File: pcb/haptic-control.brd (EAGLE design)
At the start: 40 x 160 mm, 134 parts, among them M1 SPH0641LM4H-1, P1 2P-PAD_1X3.5, P2 2P-PAD_1X3.5, P3 2P-PAD_1X3.5, P4 2P-PAD_1X3.5, U1 MIC23159, U10 DRV2605L, U11 DRV2605L, U12 MTCH6301, U2 BQ51050B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

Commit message: silkscreen experiments
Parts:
- moved U$3 1.80 mm to (35.5, 16.0)
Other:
- outline, holes or cut-outs redrawn
- board text added: "HapticControl V0.1 1920"
- board text removed: "1920"

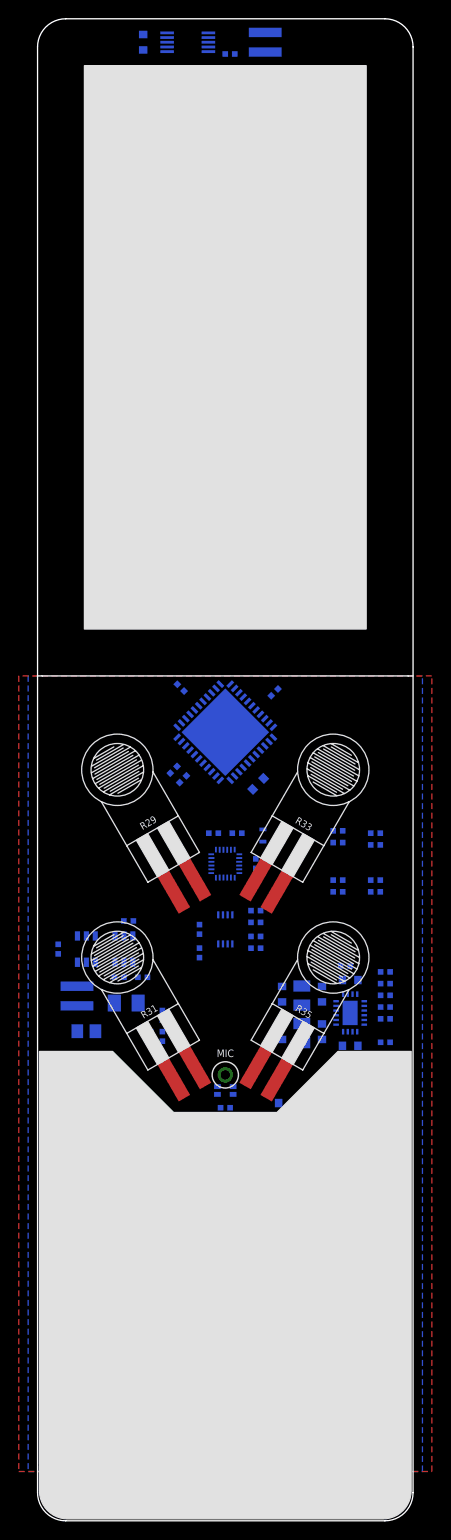
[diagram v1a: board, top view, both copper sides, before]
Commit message: Add pcap touch panel
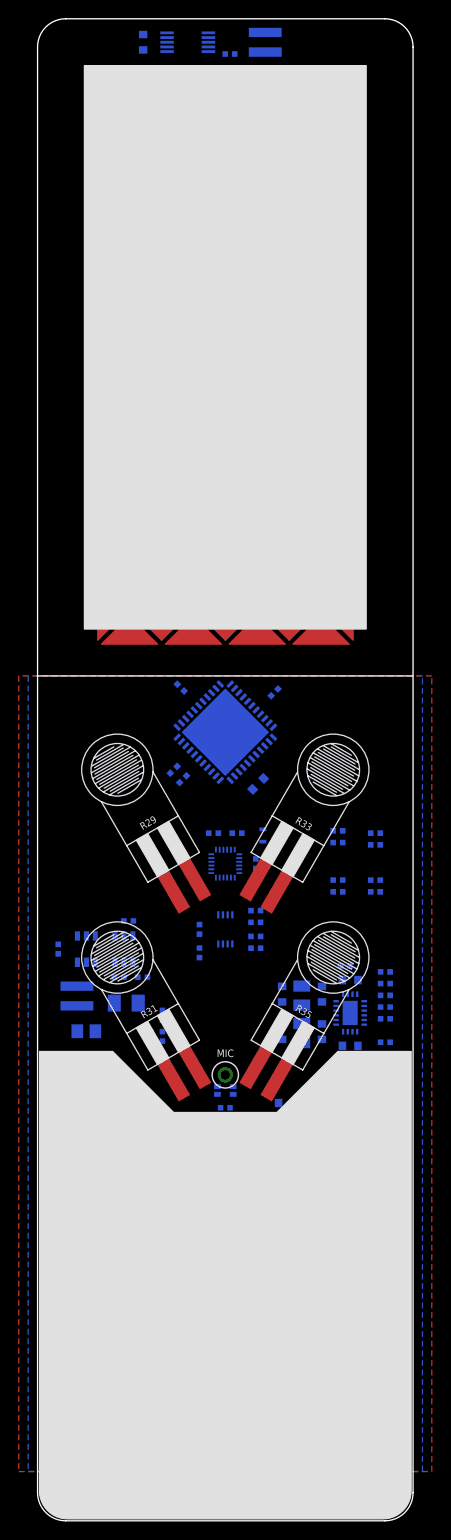
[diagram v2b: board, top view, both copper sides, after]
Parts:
- added MAT-X1, MAT-X2, MAT-X3, MAT-X4: X_9P, Touch Panel:TOUCH_X_9P
- added MAT-Y1, MAT-Y2, MAT-Y3, MAT-Y4, MAT-Y5, MAT-Y6, MAT-Y7, MAT-Y8, MAT-Y9: Y_4P, Touch Panel:TOUCH_Y_4P
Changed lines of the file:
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@@
 <drawing>
 <settings>
-<setting alwaysvectorfont="yes"/>
+<setting alwaysvectorfont="no"/>
 <setting verticaltext="up"/>
 </settings>
@@
 <layer number="155" name="FabDoc3" color="7" fill="1" visible="yes" active="yes"/>
 <layer number="160" name="O_Dim" color="12" fill="11" visible="yes" active="yes"/>
+<layer number="166" name="AntennaArea" color="7" fill="1" visible="no" active="yes"/>
+<layer number="168" name="4mmHeightArea" color="7" fill="1" visible="no" active="yes"/>
 <layer number="191" name="mNets" color="7" fill="1" visible="yes" active="yes"/>
 <layer number="192" name="mBusses" color="7" fill="1" visible="yes" active="yes"/>
@@
 <wire x1="37.1" y1="31.8" x2="39.5" y2="31.8" width="0.1524" layer="22"/>
 <wire x1="38.3" y1="41.8" x2="38.3" y2="29.4" width="0.1524" layer="22"/>
-<wire x1="0" y1="90" x2="0.5" y2="90" width="0.1524" layer="21"/>
 <text x="6" y="78.5" size="1.75" layer="22" font="vector" ratio="15" rot="MR270" align="center">HapticControl
 V0.1 1920</text>
@@
 <vertex x="0.2" y="3.2"/>
 </polygon>
-<wire x1="0.5" y1="90" x2="39.5" y2="90" width="0.1524" layer="21"/>
-<wire x1="39.5" y1="90" x2="40" y2="90" width="0.1524" layer="21"/>
+<wire x1="0" y1="90" x2="40" y2="90" width="0.1524" layer="21"/>
 <wire x1="0.5" y1="50" x2="39.5" y2="50" width="0.127" layer="22"/>
 <wire x1="39.5" y1="90" x2="0.5" y2="90" width="0.127" layer="22"/>
@@
 </element>
 <element name="U$3" library="Utility &gt; Silkscreen" package="DESIGNEDINPT" value="" x="35.5" y="16" smashed="yes" rot="MR90"/>
+<element name="MAT-X1" library="Touch Panel" package="TOUCH_X_9P" value="X_9P" x="9.8" y="124" smashed="yes"/>
+<element name="MAT-X2" library="Touch Panel" package="TOUCH_X_9P" value="X_9P" x="16.6" y="124" smashed="yes"/>
+<element name="MAT-X3" library="Touch Panel" package="TOUCH_X_9P" value="X_9P" x="23.4" y="124" smashed="yes"/>
+<element name="MAT-X4" library="Touch Panel" package="TOUCH_X_9P" value="X_9P" x="30.2" y="124" smashed="yes"/>
+<element name="MAT-Y1" library="Touch Panel" package="TOUCH_Y_4P" value="Y_4P" x="19.975" y="151.175" smashed="yes"/>
+<element name="MAT-Y2" library="Touch Panel" package="TOUCH_Y_4P" value="Y_4P" x="19.975" y="144.375" smashed="yes"/>
+<element name="MAT-Y3" library="Touch Panel" package="TOUCH_Y_4P" value="Y_4P" x="19.975" y="137.575" smashed="yes"/>
+<element name="MAT-Y4" library="Touch Panel" package="TOUCH_Y_4P" value="Y_4P" x="19.975" y="130.775" smashed="yes"/>
+<element name="MAT-Y5" library="Touch Panel" package="TOUCH_Y_4P" value="Y_4P" x="19.975" y="123.975" smashed="yes"/>
+<element name="MAT-Y6" library="Touch Panel" package="TOUCH_Y_4P" value="Y_4P" x="19.975" y="117.15" smashed="yes"/>
+<element name="MAT-Y7" library="Touch Panel" package="TOUCH_Y_4P" value="Y_4P" x="19.975" y="110.375" smashed="yes"/>
+<element name="MAT-Y8" library="Touch Panel" package="TOUCH_Y_4P" value="Y_4P" x="19.975" y="103.575" smashed="yes"/>
+<element name="MAT-Y9" library="Touch Panel" package="TOUCH_Y_4P" value="Y_4P" x="19.975" y="96.775" smashed="yes"/>
 </elements>
 <signals>

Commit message: Updated FSR package with provided design dimensions
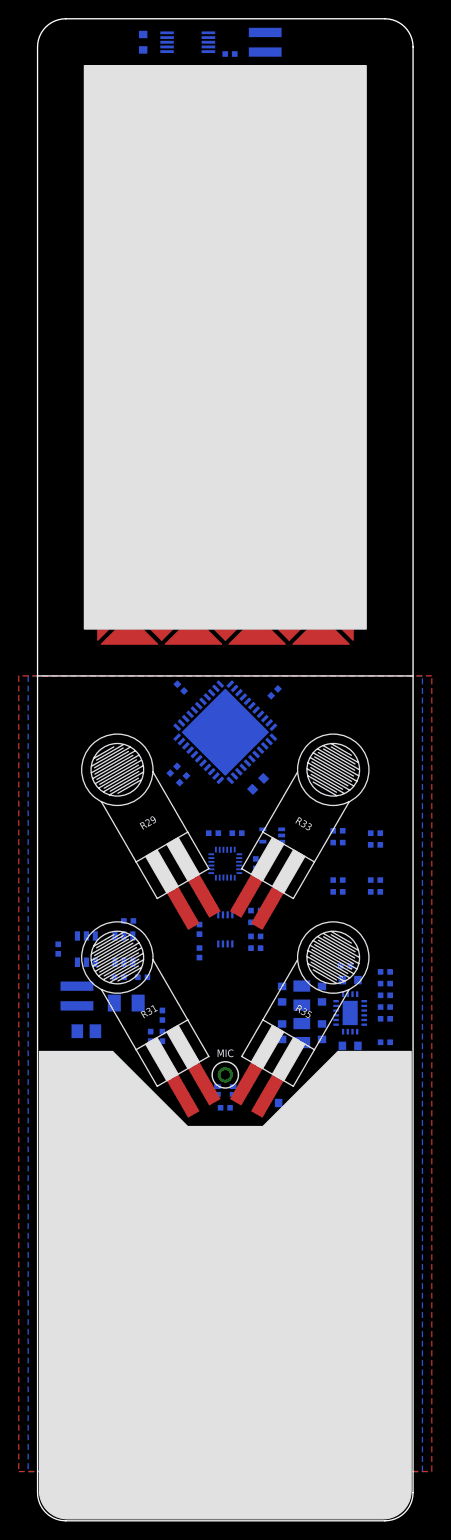
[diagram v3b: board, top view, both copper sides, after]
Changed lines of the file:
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@@
 <vertex x="0.2" y="50"/>
 <vertex x="8" y="50"/>
-<vertex x="14.5" y="43.5"/>
-<vertex x="25.5" y="43.5"/>
+<vertex x="16" y="42"/>
+<vertex x="24" y="42"/>
 <vertex x="32" y="50"/>
 <vertex x="39.8" y="50"/>
@@
 <wire x1="14.140790625" y1="79.6407875" x2="15.8592125" y2="79.359209375" width="0" layer="19" extent="16-16"/>
 <wire x1="26" y1="72.35" x2="15.8592125" y2="79.359209375" width="0" layer="19" extent="16-16"/>
-<wire x1="23.224165625" y1="68.265834375" x2="26" y2="72.35" width="0" layer="19" extent="1-16"/>
-<wire x1="23.758" y1="62.25" x2="23.224165625" y2="68.265834375" width="0" layer="19" extent="1-16"/>
+<wire x1="22.224165625" y1="66.533784375" x2="26" y2="72.35" width="0" layer="19" extent="1-16"/>
+<wire x1="23.758" y1="62.25" x2="22.224165625" y2="66.533784375" width="0" layer="19" extent="1-16"/>
 <wire x1="23.758" y1="61" x2="23.758" y2="62.25" width="0" layer="19" extent="16-16"/>
 <wire x1="17.25" y1="59.992" x2="23.758" y2="61" width="0" layer="19" extent="16-16"/>
-<wire x1="14.524165625" y1="66.965834375" x2="17.25" y2="59.992" width="0" layer="19" extent="1-16"/>
+<wire x1="15.524165625" y1="65.233784375" x2="17.25" y2="59.992" width="0" layer="19" extent="1-16"/>
 <wire x1="26.05" y1="51.277" x2="23.758" y2="61" width="0" layer="19" extent="16-16"/>
 <wire x1="28.15" y1="50.934" x2="26.05" y2="51.277" width="0" layer="19" extent="16-16"/>
-<wire x1="23.224165625" y1="48.265834375" x2="26.05" y2="51.277" width="0" layer="19" extent="1-16"/>
-<wire x1="20.8375" y1="45.426" x2="23.224165625" y2="48.265834375" width="0" layer="19" extent="1-16"/>
+<wire x1="22.224165625" y1="46.533784375" x2="26.05" y2="51.277" width="0" layer="19" extent="1-16"/>
+<wire x1="20.8375" y1="45.426" x2="22.224165625" y2="46.533784375" width="0" layer="19" extent="1-16"/>
 <wire x1="20.508" y1="44" x2="20.8375" y2="45.426" width="0" layer="19" extent="16-16"/>
 <wire x1="34.05" y1="52.1" x2="28.15" y2="50.934" width="0" layer="19" extent="16-16"/>
@@
 <wire x1="27.323" y1="44.5" x2="28.15" y2="50.934" width="0" layer="19" extent="16-16"/>
 <wire x1="26.5" y1="42.7" x2="27.323" y2="44.5" width="0" layer="19" extent="16-16"/>
-<wire x1="14.524165625" y1="46.965834375" x2="20.8375" y2="45.426" width="0" layer="19" extent="1-16"/>
-<wire x1="10.9" y1="44.708" x2="14.524165625" y2="46.965834375" width="0" layer="19" extent="1-16"/>
+<wire x1="15.524165625" y1="45.233784375" x2="20.8375" y2="45.426" width="0" layer="19" extent="1-16"/>
+<wire x1="10.9" y1="44.708" x2="15.524165625" y2="45.233784375" width="0" layer="19" extent="1-16"/>
 <wire x1="32.215" y1="31.96" x2="26.5" y2="42.7" width="0" layer="19" extent="16-16"/>
 <wire x1="11.1" y1="21.808" x2="10.9" y2="44.708" width="0" layer="19" extent="16-16"/>
@@
 <contactref element="U5" pad="39"/>
 <wire x1="36.508" y1="73.25" x2="36.508" y2="72" width="0" layer="19" extent="16-16"/>
-<wire x1="16.77583125" y1="68.265834375" x2="36.508" y2="72" width="0" layer="19" extent="1-16"/>
-<wire x1="23.53" y1="27.875" x2="16.77583125" y2="68.265834375" width="0" layer="19" extent="1-16"/>
+<wire x1="17.77583125" y1="66.533784375" x2="36.508" y2="72" width="0" layer="19" extent="1-16"/>
+<wire x1="23.53" y1="27.875" x2="17.77583125" y2="66.533784375" width="0" layer="19" extent="1-16"/>
 </signal>
 <signal name="FSR_CH_N">
@@
 <contactref element="U5" pad="38"/>
 <wire x1="36.508" y1="68.25" x2="36.508" y2="67" width="0" layer="19" extent="16-16"/>
-<wire x1="16.77583125" y1="48.265834375" x2="36.508" y2="67" width="0" layer="19" extent="1-16"/>
-<wire x1="23.53" y1="28.375" x2="16.77583125" y2="48.265834375" width="0" layer="19" extent="1-16"/>
+<wire x1="17.77583125" y1="46.533784375" x2="36.508" y2="67" width="0" layer="19" extent="1-16"/>
+<wire x1="23.53" y1="28.375" x2="17.77583125" y2="46.533784375" width="0" layer="19" extent="1-16"/>
 </signal>
 <signal name="FSR_VOL_P">
@@
 <contactref element="U5" pad="40"/>
 <wire x1="32.508" y1="73.5" x2="32.508" y2="72.25" width="0" layer="19" extent="16-16"/>
-<wire x1="25.47583125" y1="66.965834375" x2="32.508" y2="72.25" width="0" layer="19" extent="1-16"/>
-<wire x1="23.53" y1="27.375" x2="25.47583125" y2="66.965834375" width="0" layer="19" extent="1-16"/>
+<wire x1="24.47583125" y1="65.233784375" x2="32.508" y2="72.25" width="0" layer="19" extent="1-16"/>
+<wire x1="23.53" y1="27.375" x2="24.47583125" y2="65.233784375" width="0" layer="19" extent="1-16"/>
 </signal>
 <signal name="FSR_VOL_N">
@@
 <contactref element="U5" pad="37"/>
 <wire x1="32.508" y1="68.25" x2="32.508" y2="67" width="0" layer="19" extent="16-16"/>
-<wire x1="25.47583125" y1="46.965834375" x2="32.508" y2="67" width="0" layer="19" extent="1-16"/>
-<wire x1="23.53" y1="28.875" x2="25.47583125" y2="46.965834375" width="0" layer="19" extent="1-16"/>
+<wire x1="24.47583125" y1="45.233784375" x2="32.508" y2="67" width="0" layer="19" extent="1-16"/>
+<wire x1="23.53" y1="28.875" x2="24.47583125" y2="45.233784375" width="0" layer="19" extent="1-16"/>
 </signal>
 <signal name="FLASH_SCK">

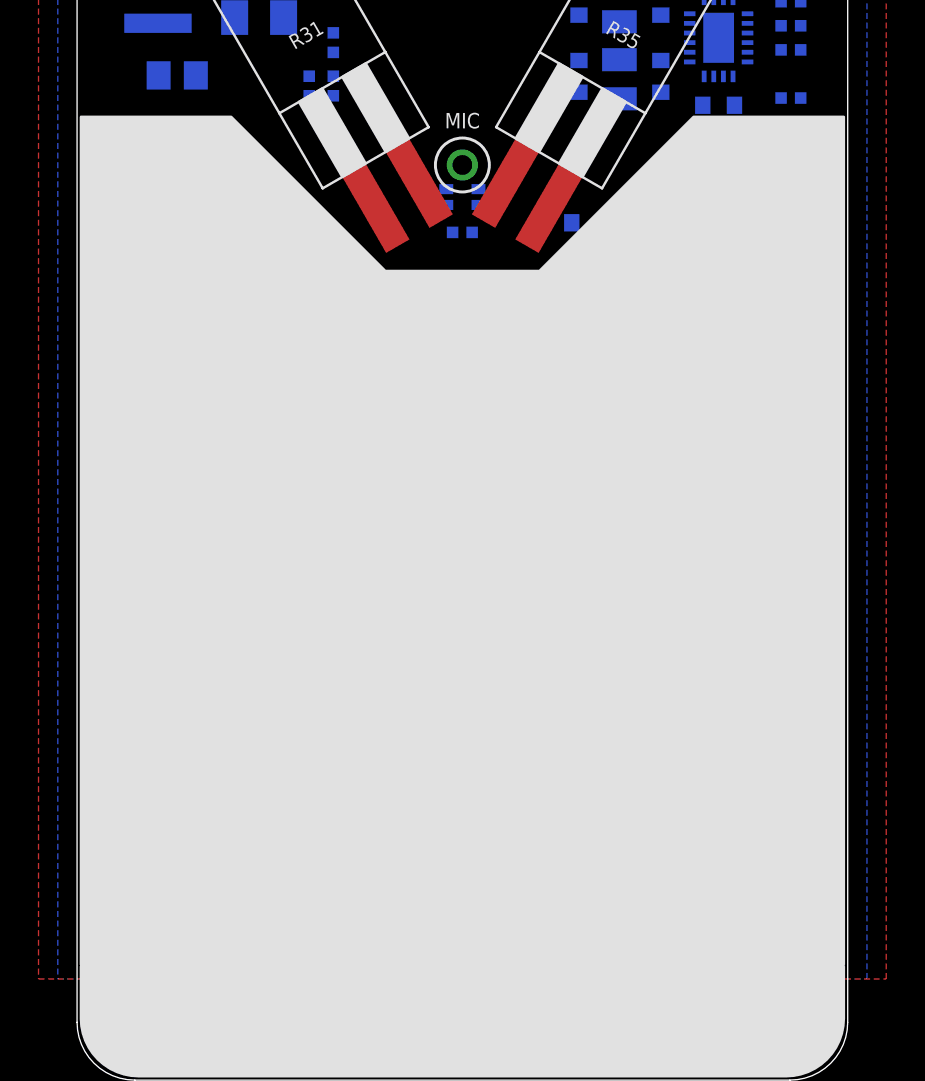
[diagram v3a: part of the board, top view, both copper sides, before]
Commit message: Added IPL logo
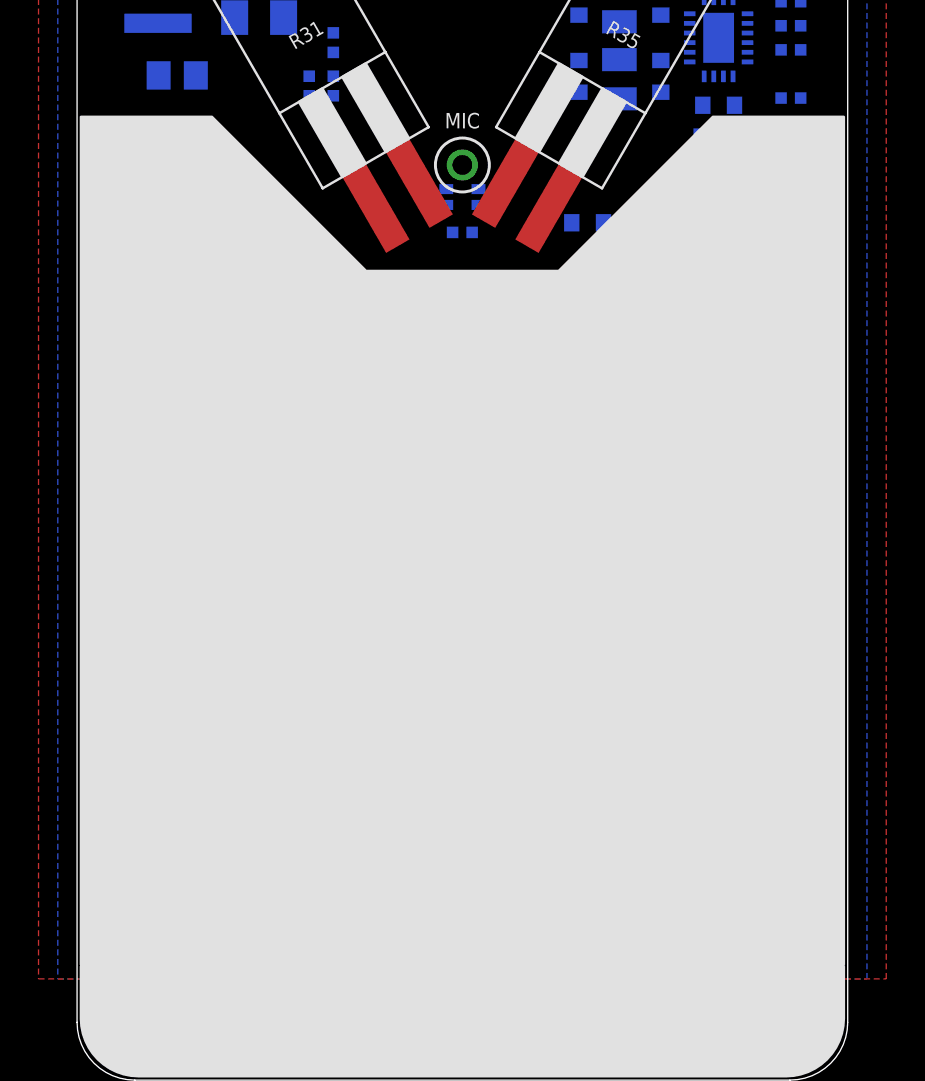
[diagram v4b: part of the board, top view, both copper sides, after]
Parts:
- added LOGO1: IPL-10MM, Silkscreen:IPL_10MM
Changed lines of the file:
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@@
 <drawing>
 <settings>
-<setting alwaysvectorfont="no"/>
+<setting alwaysvectorfont="yes"/>
 <setting verticaltext="up"/>
 </settings>
@@
 <vertex x="0.2" y="6"/>
 <vertex x="0.2" y="50"/>
-<vertex x="8" y="50"/>
-<vertex x="16" y="42"/>
-<vertex x="24" y="42"/>
-<vertex x="32" y="50"/>
+<vertex x="7" y="50"/>
+<vertex x="15" y="42"/>
+<vertex x="25" y="42"/>
+<vertex x="33" y="50"/>
 <vertex x="39.8" y="50"/>
 <vertex x="39.8" y="6"/>
@@
 <element name="MAT-Y8" library="Touch Panel" package="TOUCH_Y_4P" value="Y_4P" x="19.975" y="103.575" smashed="yes"/>
 <element name="MAT-Y9" library="Touch Panel" package="TOUCH_Y_4P" value="Y_4P" x="19.975" y="96.775" smashed="yes"/>
+<element name="LOGO1" library="Silkscreen" package="IPL_10MM" value="IPL-10MM" x="35.5" y="87" smashed="yes" rot="MR270"/>
 </elements>
 <signals>
